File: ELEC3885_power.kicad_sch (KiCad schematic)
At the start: 0 parts

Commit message: Rev3 PCB layout started
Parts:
- added C13, C14: 4u7, symbol Device:C_Small
- added C19, C20: 22u, symbol Device:C_Small
- added D10: LED, symbol Device:LED
- added D11: SS34, symbol Device:D_Schottky
- added D9: uClamp0571P, symbol Device:D
- added J6: Conn_LiPo, symbol Connector:Conn_01x02_Socket
- added J7: USB_B_Micro, symbol Connector:USB_B_Micro
- added L1: 22uH, symbol Device:L
- added R4, R50: 2k, symbol Device:R
- added R48: R, symbol Device:R
- added R49: 15k, symbol Device:R
- added U10: MT3608, Package_TO_SOT_SMD:SOT-23-6, symbol Regulator_Switching:MT3608
- added U11: L7805, symbol Regulator_Linear:L7805
- added U9: MCP73831-2-OT, Package_TO_SOT_SMD:SOT-23-5, symbol Battery_Management:MCP73831-2-OT
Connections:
- new net: R4.1, U9.5 (PROG)
- new net: C14.1, C19.1, J6.1 (Pin_1), L1.1, U10.4 (EN), U10.5 (IN), U9.3 (V_{BAT})
- new net: D10.1 (K), U9.1 (STAT)
- new net: D10.2 (A), R48.2
- new net: C20.1, D11.1 (K), R49.1, U11.1 (IN)
- new net: D11.2 (A), L1.2, U10.1 (SW)
- new net: R49.2, R50.1, U10.3 (FB)
- new net: C13.1, D9.1 (K), J7.1 (VBUS), R48.1, U9.4 (V_{DD})
- new net +5V: U11.3 (OUT)
- new net GND: C13.2, C14.2, C19.2, C20.2, D9.2 (A), J6.2 (Pin_2), J7.5 (GND), J7.6 (Shield), R4.2, R50.2, U10.2 (GND), U11.2 (GND), U9.2 (V_{SS})

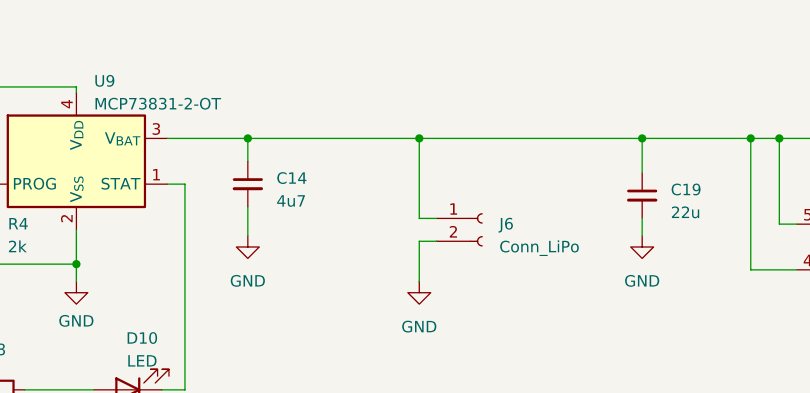
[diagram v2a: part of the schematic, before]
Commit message: Rev3 rework, diff amp jumpers added
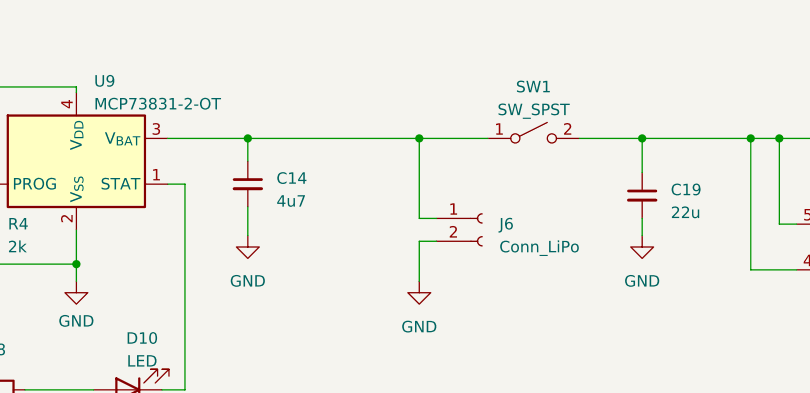
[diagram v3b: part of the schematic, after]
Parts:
- added SW1: SW_SPST, Button_Switch_THT:SW_CuK_OS102011MA1QN1_SPDT_Angled, symbol Switch:SW_SPST
- C13, C14: footprint (none) -> Capacitor_SMD:C_0402_1005Metric
- C19, C20: footprint (none) -> Capacitor_SMD:C_0603_1608Metric
- D10: footprint (none) -> LED_SMD:LED_0201_0603Metric
- D11: footprint (none) -> Diode_SMD:D_SMC
- D9: footprint (none) -> Luke_library:DFN1610-2
- J6: footprint (none) -> Connector_JST:JST_EH_S2B-EH_1x02_P2.50mm_Horizontal
- J7: footprint (none) -> Connector_USB:USB_Micro-B_Amphenol_10103594-0001LF_Horizontal
- L1: footprint (none) -> Inductor_SMD:L_6.3x6.3_H3
- R4, R48, R50: footprint (none) -> Resistor_SMD:R_0402_1005Metric
- R49: footprint (none) -> Resistor_SMD:R_0603_1608Metric
- U11: footprint (none) -> Package_TO_SOT_SMD:TO-252-2
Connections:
- net at C19.1, L1.1, U10.4 (EN)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: now also SW1.2 (B); no longer C14.1, J6.1 (Pin_1), U9.3 (V_{BAT})
- new net: C14.1, J6.1 (Pin_1), SW1.1 (A), U9.3 (V_{BAT})
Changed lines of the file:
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@@
   (junction (at 182.88 59.055) (diameter 0) (color 0 0 0 0)
   )
+  (junction (at 133.35 32.385) (diameter 0) (color 0 0 0 0)
+  )
   (junction (at 192.405 32.385) (diameter 0) (color 0 0 0 0)
   )
@@
   (junction (at 24.765 43.815) (diameter 0) (color 0 0 0 0)
   )
-  (junction (at 133.35 32.385) (diameter 0) (color 0 0 0 0)
-  )
   (junction (at 78.105 26.67) (diameter 0) (color 0 0 0 0)
   )
@@
     (stroke (width 0) (type default))
   )
+  (wire (pts (xy 151.13 32.385) (xy 158.115 32.385))
+    (stroke (width 0) (type default))
+  )
   (wire (pts (xy 158.115 36.195) (xy 158.115 32.385))
     (stroke (width 0) (type default))
@@
     (stroke (width 0) (type default))
   )
-  (wire (pts (xy 133.35 32.385) (xy 158.115 32.385))
-    (stroke (width 0) (type default))
-  )
   (wire (pts (xy 81.915 60.325) (xy 78.105 60.325))
     (stroke (width 0) (type default))
@@
     (stroke (width 0) (type default))
   )
+  (wire (pts (xy 133.35 32.385) (xy 140.97 32.385))
+    (stroke (width 0) (type default))
+  )
   (wire (pts (xy 190.5 46.99) (xy 201.93 46.99))
     (stroke (width 0) (type default))
@@
     (stroke (width 0) (type default))
   )
-  (wire (pts (xy 114.3 32.385) (xy 105.41 32.385))
+  (wire (pts (xy 105.41 32.385) (xy 114.3 32.385))
     (stroke (width 0) (type default))
   )
@@
       (effects (font (size 1.27 1.27)) (justify left))
     )
-    (property "Footprint" "" (at 83.312 42.545 90)
+    (property "Footprint" "Resistor_SMD:R_0402_1005Metric" (at 83.312 42.545 90)
       (effects (font (size 1.27 1.27)) hide)
     )
@@
       (effects (font (size 1.27 1.27)) (justify left))
     )
-    (property "Footprint" "" (at 140.335 41.275 0)
+    (property "Footprint" "Connector_JST:JST_EH_S2B-EH_1x02_P2.50mm_Horizontal" (at 140.335 41.275 0)
       (effects (font (size 1.27 1.27)) hide)
     )
@@
       (effects (font (size 1.27 1.27)))
     )
-    (property "Footprint" "" (at 100.965 60.325 0)
+    (property "Footprint" "LED_SMD:LED_0201_0603Metric" (at 100.965 60.325 0)
       (effects (font (size 1.27 1.27)) hide)
     )
@@
       (effects (font (size 1.27 1.27)))
     )
-    (property "Footprint" "" (at 230.505 36.195 0)
+    (property "Footprint" "Package_TO_SOT_SMD:TO-252-2" (at 230.505 36.195 0)
       (effects (font (size 1.27 1.27) italic) (justify left) hide)
     )
@@
       (effects (font (size 1.27 1.27)))
     )
-    (property "Footprint" "" (at 196.85 32.385 0)
+    (property "Footprint" "Diode_SMD:D_SMC" (at 196.85 32.385 0)
       (effects (font (size 1.27 1.27)) hide)
     )
@@
       (effects (font (size 1.27 1.27)) (justify left))
     )
-    (property "Footprint" "" (at 200.152 40.005 90)
+    (property "Footprint" "Resistor_SMD:R_0603_1608Metric" (at 200.152 40.005 90)
       (effects (font (size 1.27 1.27)) hide)
     )
@@
     )
   )
+  (symbol (lib_id "Switch:SW_SPST") (at 146.05 32.385 0) (unit 1)
+    (in_bom yes) (on_board yes) (dnp no) (fields_autoplaced)
+    (property "Reference" "SW1" (at 146.05 26.67 0)
+      (effects (font (size 1.27 1.27)))
+    )
+    (property "Value" "SW_SPST" (at 146.05 29.21 0)
+      (effects (font (size 1.27 1.27)))
+    )
+    (property "Footprint" "Button_Switch_THT:SW_CuK_OS102011MA1QN1_SPDT_Angled" (at 146.05 32.385 0)
+      (effects (font (size 1.27 1.27)) hide)
+    )
+    (property "Datasheet" "~" (at 146.05 32.385 0)
+      (effects (font (size 1.27 1.27)) hide)
+    )
+    (pin "1")
+    (pin "2")
+    (instances
+      (project "ELEC3885"
+        (path "/eaef1172-3351-417c-bfc4-74a598f141cb/efdad2b4-cd57-4c95-97e8-5b864f2cd9b4"
+          (reference "SW1") (unit 1)
+        )
+      )
+    )
+  )
   (symbol (lib_id "power:GND") (at 45.085 38.1 0) (unit 1)
     (in_bom yes) (on_board yes) (dnp no) (fields_autoplaced)
@@
       (effects (font (size 1.27 1.27)))
     )
-    (property "Footprint" "" (at 85.725 62.103 90)
+    (property "Footprint" "Resistor_SMD:R_0402_1005Metric" (at 85.725 62.103 90)
       (effects (font (size 1.27 1.27)) hide)
     )
@@
       (effects (font (size 1.27 1.27)) (justify left))
     )
-    (property "Footprint" "" (at 45.085 30.48 0)
+    (property "Footprint" "Luke_library:DFN1610-2" (at 45.085 30.48 0)
       (effects (font (size 1.27 1.27)) hide)
     )
@@
       (effects (font (size 1.27 1.27)) (justify left))
     )
-    (property "Footprint" "" (at 200.152 53.34 90)
+    (property "Footprint" "Resistor_SMD:R_0402_1005Metric" (at 200.152 53.34 90)
       (effects (font (size 1.27 1.27)) hide)
     )
@@
       (effects (font (size 1.27 1.27)))
     )
-    (property "Footprint" "" (at 182.88 32.385 0)
+    (property "Footprint" "Inductor_SMD:L_6.3x6.3_H3" (at 182.88 32.385 0)
       (effects (font (size 1.27 1.27)) hide)
     )
@@
       (effects (font (size 1.27 1.27)) (justify left))
     )
-    (property "Footprint" "" (at 114.3 37.465 0)
+    (property "Footprint" "Capacitor_SMD:C_0402_1005Metric" (at 114.3 37.465 0)
       (effects (font (size 1.27 1.27)) hide)
     )
@@
       (effects (font (size 1.27 1.27)) (justify left))
     )
-    (property "Footprint" "" (at 64.135 31.115 0)
+    (property "Footprint" "Capacitor_SMD:C_0402_1005Metric" (at 64.135 31.115 0)
       (effects (font (size 1.27 1.27)) hide)
     )
@@
       (effects (font (size 1.27 1.27)) (justify left))
     )
-    (property "Footprint" "" (at 211.455 38.1 0)
+    (property "Footprint" "Capacitor_SMD:C_0603_1608Metric" (at 211.455 38.1 0)
       (effects (font (size 1.27 1.27)) hide)
     )
@@
       (effects (font (size 1.27 1.27)))
     )
-    (property "Footprint" "" (at 29.845 33.02 0)
+    (property "Footprint" "Connector_USB:USB_Micro-B_Amphenol_10103594-0001LF_Horizontal" (at 29.845 33.02 0)
       (effects (font (size 1.27 1.27)) hide)
     )
@@
       (effects (font (size 1.27 1.27)) (justify left))
     )
-    (property "Footprint" "" (at 158.115 38.735 0)
-      (effects (font (size 1.27 1.27)) hide)
-    )
+    (property "Footprint" "Capacitor_SMD:C_0603_1608Metric" (at 158.115 38.735 0)
+      (effects (font (size 1.27 1.27)) hide)
+    )

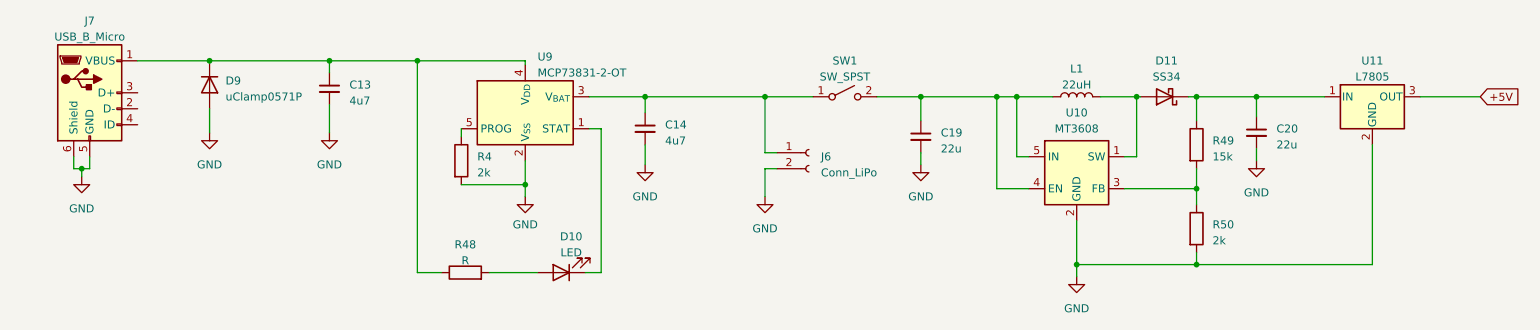
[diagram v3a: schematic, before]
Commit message: Encoders, RGB LED added, PCB cleanup
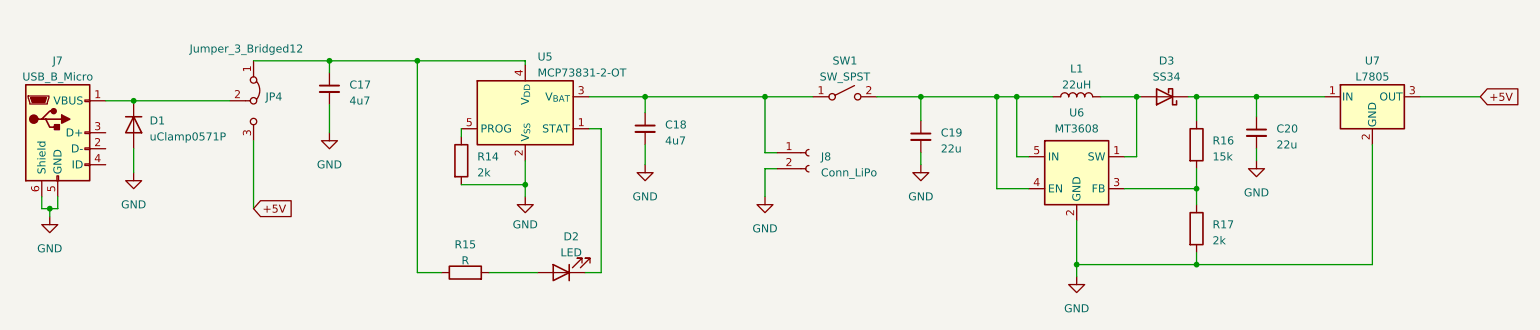
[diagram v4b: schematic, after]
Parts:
- added JP4: Jumper_3_Bridged12, Jumper:SolderJumper-3_P1.3mm_Bridged2Bar12_RoundedPad1.0x1.5mm_NumberLabels, symbol Jumper:Jumper_3_Bridged12
- renumbered C13 to C17, C14 to C18, D9 to D1, D10 to D2, D11 to D3, J6 to J8, R4 to R14, R48 to R15, R49 to R16, R50 to R17, U9 to U5, U10 to U6, U11 to U7
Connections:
- net +5V: now also JP4.3 (B)
- net at C17.1, R15.1, U5.4 (V_{DD}): now also JP4.1 (A); no longer D1.1 (K), J7.1 (VBUS)
- new net: D1.1 (K), J7.1 (VBUS), JP4.2 (C)
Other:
- moved on the sheet: D1, J7

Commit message: Footprints updated except codec
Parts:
- C17, C18: footprint Capacitor_SMD:C_0402_1005Metric -> Capacitor_SMD:C_0603_1608Metric
- D2: footprint LED_SMD:LED_0201_0603Metric -> LED_SMD:LED_0603_1608Metric
- L1: footprint Inductor_SMD:L_6.3x6.3_H3 -> Inductor_SMD:L_10.4x10.4_H4.8
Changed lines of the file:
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@@
       (effects (font (size 1.27 1.27)))
     )
-    (property "Footprint" "LED_SMD:LED_0201_0603Metric" (at 100.965 60.325 0)
+    (property "Footprint" "LED_SMD:LED_0603_1608Metric" (at 100.965 60.325 0)
       (effects (font (size 1.27 1.27)) hide)
     )
@@
       (effects (font (size 1.27 1.27)))
     )
-    (property "Footprint" "Inductor_SMD:L_6.3x6.3_H3" (at 182.88 32.385 0)
+    (property "Footprint" "Inductor_SMD:L_10.4x10.4_H4.8" (at 182.88 32.385 0)
       (effects (font (size 1.27 1.27)) hide)
     )
@@
       (effects (font (size 1.27 1.27)) (justify left))
     )
-    (property "Footprint" "Capacitor_SMD:C_0402_1005Metric" (at 114.3 37.465 0)
+    (property "Footprint" "Capacitor_SMD:C_0603_1608Metric" (at 114.3 37.465 0)
       (effects (font (size 1.27 1.27)) hide)
     )
@@
       (effects (font (size 1.27 1.27)) (justify left))
     )
-    (property "Footprint" "Capacitor_SMD:C_0402_1005Metric" (at 64.135 31.115 0)
-      (effects (font (size 1.27 1.27)) hide)
-    )
+    (property "Footprint" "Capacitor_SMD:C_0603_1608Metric" (at 64.135 31.115 0)
+      (effects (font (size 1.27 1.27)) hide)
+    )

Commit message: Rev4 ordered
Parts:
- J7: footprint Connector_USB:USB_Micro-B_Amphenol_10103594-0001LF_Horizontal -> Luke_library:USB_Micro-B_MicroXNJ_Horizontal
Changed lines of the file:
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@@
       (effects (font (size 1.27 1.27)))
     )
-    (property "Footprint" "Connector_USB:USB_Micro-B_Amphenol_10103594-0001LF_Horizontal" (at 24.765 39.37 0)
+    (property "Footprint" "Luke_library:USB_Micro-B_MicroXNJ_Horizontal" (at 24.765 39.37 0)
       (effects (font (size 1.27 1.27)) hide)
     )
